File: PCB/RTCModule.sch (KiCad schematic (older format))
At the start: 0 parts

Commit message: Updated the schematic for the RTC and controller
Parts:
- added Q? (x7): IRLML2502, Micro3, symbol IRLML2502
- added Q?: NOPOP, Micro3, symbol IRLML2502
- added R? (x7): 10K, symbol R
- added R? (x2): 1K5, symbol R
- added R? (x5): 4K7, symbol R
- added R? (x2): NOPOP, symbol R
- added U?: RTC-DCF77, symbol RTC-DCF77
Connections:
- new net: Q?.3 (D), R?.2
- new net ALARM_INT: Q?.2 (S), Q?.3 (D), R?.2, R?.2, U?.10 (MOSI)
- new net DCF_RCPT: Q?.2 (S), Q?.3 (D), R?.2, R?.2, U?.8 (~SS)
- new net GND: U?.12 (GND), U?.6 (GND)
- new net MISO: Q?.2 (S), Q?.3 (D), R?.2, R?.2, U?.5 (Tx)
- new net MOSI: Q?.2 (S), Q?.3 (D), R?.2, R?.2, U?.4 (Rx)
- new net Periodic_INT: Q?.2 (S), Q?.3 (D), R?.2, R?.2
- new net Rx: Q?.2 (S), R?.2, U?.9 (SCK)
- new net SCK: Q?.2 (S), Q?.3 (D), R?.2, R?.2, U?.3 (SCL)
- new net Vbb: Q?.1 (G), Q?.1 (G), Q?.1 (G), Q?.1 (G), Q?.1 (G), Q?.1 (G), Q?.1 (G), Q?.1 (G), R?.1, R?.1, R?.1, R?.1, R?.1, R?.1, R?.1, R?.1, U?.1 (+Vb), U?.7 (+Vb)
- new net Vcc: R?.1, R?.1, R?.1, R?.1, R?.1, R?.1, R?.1, R?.1
- new net ~SS: Q?.2 (S), Q?.3 (D), R?.2, R?.2, U?.2 (SDA)
- no-connect marks 0 -> 1
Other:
- note added: "The RTC-DCF77 is a pre-fabricated module \nthat has two 6 contact pin headers each end. \nThis does not need any representation here \nwith respect to connectors."

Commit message: Generated the Netlist and started associating footprints
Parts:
- Q401, Q402, Q403, Q404, Q405, Q406, Q407, Q408: renamed from Q?; footprint Micro3 -> tfac-footprints:Micro3
- R401, R402, R403, R404, R405, R406, R407, R408, R409, R410, R411, R412, R413, R414, R415, R416: renamed from R?; footprint (none) -> Resistors_SMD:R_0805_HandSoldering
- U401: renamed from U?; footprint (none) -> tfac-footprints:RTC-DCF
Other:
- note added: "The RTC-DCF77 is a pre-fabricated module \nthat has two 6 contact pin headers each end. \nThis does not need any representation here \nwith respect to connectors.\n\nThis will be modelled in the foot print as two 6-pole \nthrough hole connectors\n"
- note removed: "The RTC-DCF77 is a pre-fabricated module \nthat has two 6 contact pin headers each end. \nThis does not need any representation here \nwith respect to connectors."

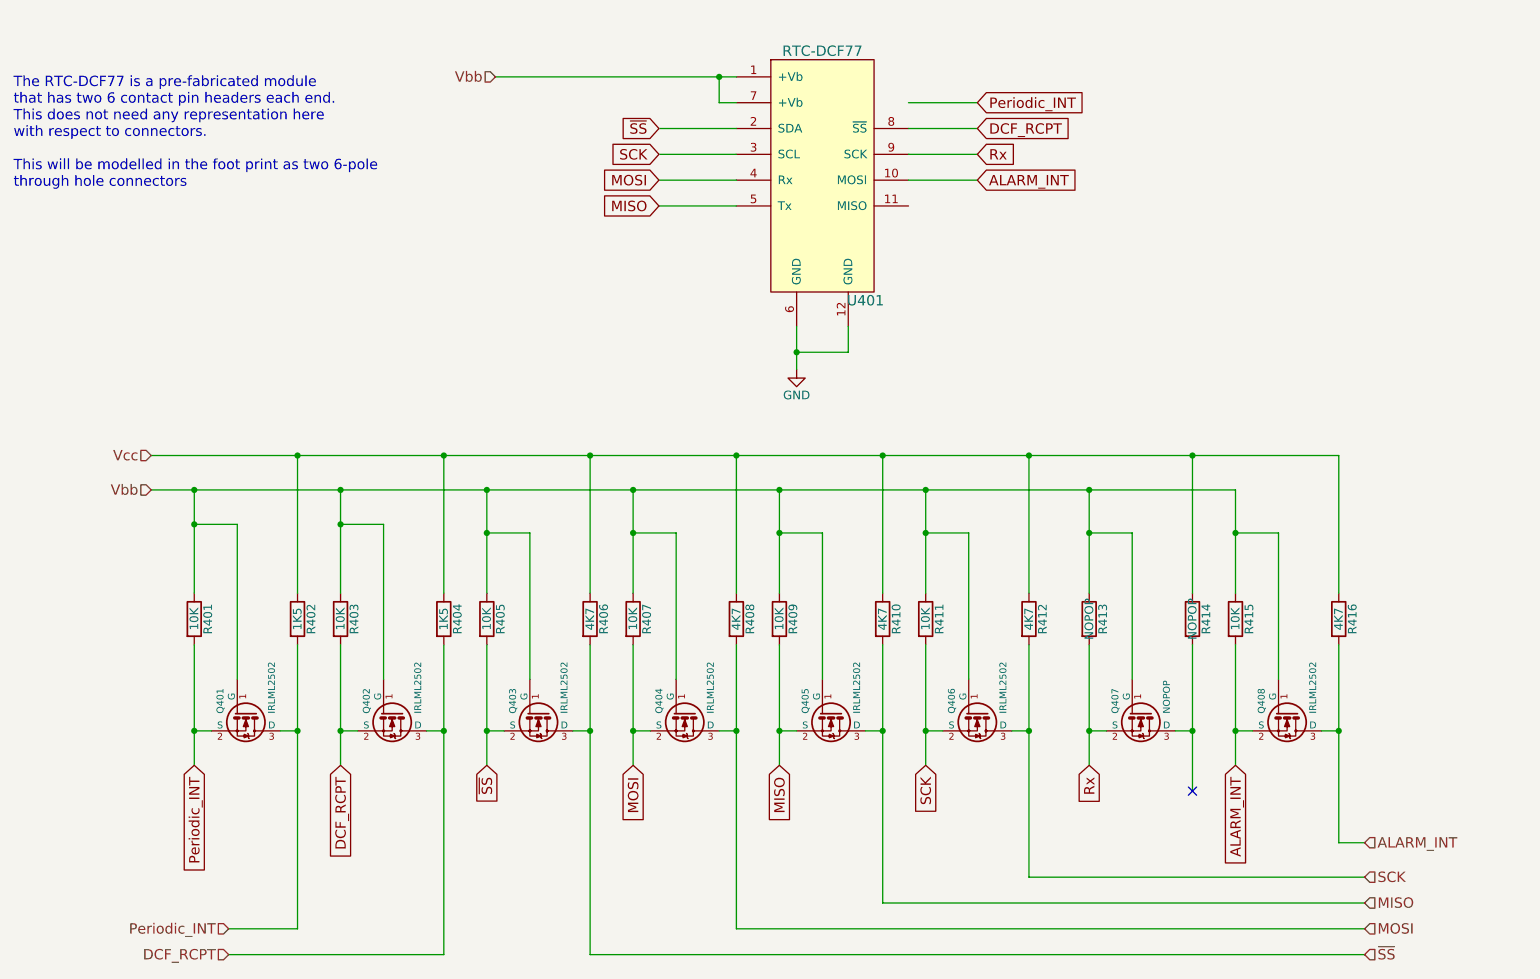
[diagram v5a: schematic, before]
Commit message: Added the switch footprints and started the layout
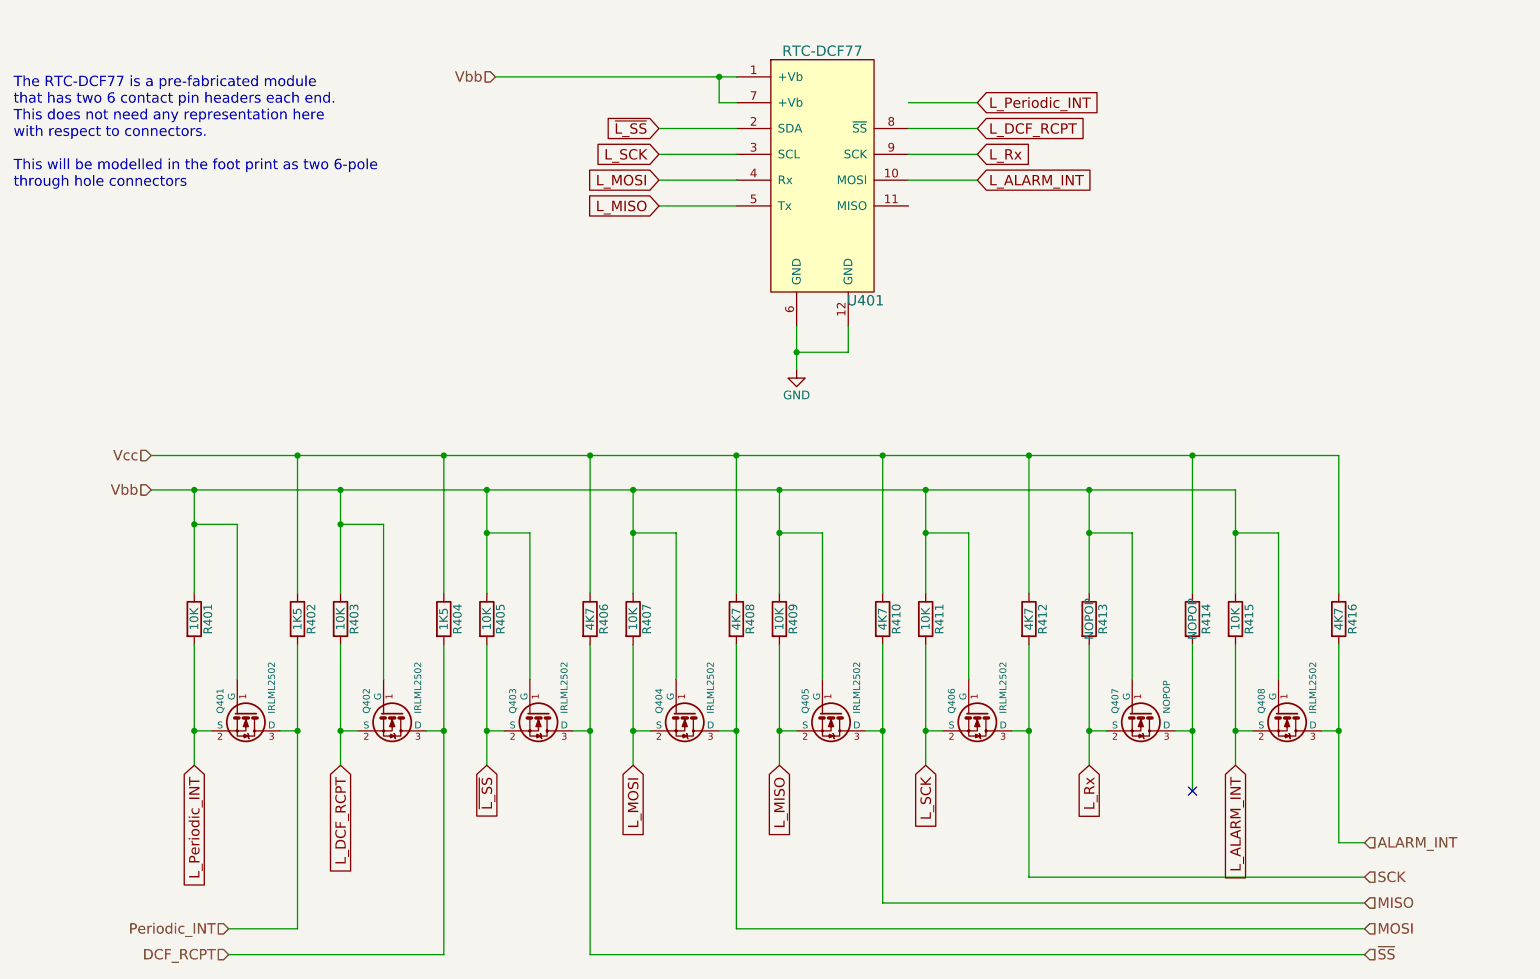
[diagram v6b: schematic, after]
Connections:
- net ALARM_INT: no longer Q408.2 (S), R415.2, U401.10 (MOSI)
- net DCF_RCPT: no longer Q402.2 (S), R403.2, U401.8 (~SS)
- net MISO: no longer Q405.2 (S), R409.2, U401.5 (Tx)
- net MOSI: no longer Q404.2 (S), R407.2, U401.4 (Rx)
- net Periodic_INT: no longer Q401.2 (S), R401.2
- net SCK: no longer Q406.2 (S), R411.2, U401.3 (SCL)
- net ~SS: no longer Q403.2 (S), R405.2, U401.2 (SDA)
- net Rx renamed L_Rx
- new net L_ALARM_INT: Q408.2 (S), R415.2, U401.10 (MOSI)
- new net L_DCF_RCPT: Q402.2 (S), R403.2, U401.8 (~SS)
- new net L_MISO: Q405.2 (S), R409.2, U401.5 (Tx)
- new net L_MOSI: Q404.2 (S), R407.2, U401.4 (Rx)
- new net L_Periodic_INT: Q401.2 (S), R401.2
- new net L_SCK: Q406.2 (S), R411.2, U401.3 (SCL)
- new net ~L_SS: Q403.2 (S), R405.2, U401.2 (SDA)
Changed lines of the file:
@@
 Vbb
 Text GLabel 2300 4950 3    60   Input ~ 0
-Periodic_INT
+L_Periodic_INT
 Text GLabel 3150 4950 3    60   Input ~ 0
-DCF_RCPT
+L_DCF_RCPT
 $Comp
 L R R405
@@
 Connection ~ 8950 4750
 Text GLabel 4000 4950 3    60   Input ~ 0
-~SS
+~L_SS
 Text GLabel 4850 4950 3    60   Input ~ 0
-MOSI
+L_MOSI
 Text GLabel 5700 4950 3    60   Input ~ 0
-MISO
+L_MISO
 Text GLabel 6550 4950 3    60   Input ~ 0
-SCK
+L_SCK
 Text GLabel 7500 4950 3    60   Input ~ 0
-Rx
+L_Rx
 Text GLabel 8350 4950 3    60   Input ~ 0
-ALARM_INT
+L_ALARM_INT
 Text GLabel 5000 1700 0    60   Input ~ 0
-MISO
+L_MISO
 Text GLabel 5000 1550 0    60   Input ~ 0
-MOSI
+L_MOSI
 Text GLabel 5000 1400 0    60   Input ~ 0
-SCK
+L_SCK
 Text GLabel 5000 1250 0    60   Input ~ 0
-~SS
+~L_SS
 Text Notes 1250 1600 0    60   ~ 0
 The RTC-DCF77 is a pre-fabricated module \nthat has two 6 contact pin headers each end. \nThis does not need any representation here \nwith respect to connectors.\n\nThis will be modelled in the foot print as two 6-pole \nthrough hole connectors\n
@@
 	6300 5750 9100 5750
 Text GLabel 6850 1100 2    60   Input ~ 0
-Periodic_INT
+L_Periodic_INT
 Text GLabel 6850 1250 2    60   Input ~ 0
-DCF_RCPT
+L_DCF_RCPT
 Text GLabel 6850 1550 2    60   Input ~ 0
-ALARM_INT
+L_ALARM_INT
 Wire Wire Line
 	6450 1100 6850 1100
@@
 	6450 1550 6850 1550
 Text GLabel 6850 1400 2    60   Input ~ 0
-Rx
+L_Rx
 Wire Wire Line
 	6450 1400 6850 1400

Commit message: Started the layout
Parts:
- added TP1, TP2: CONN_01X06, Pin_Headers:Pin_Header_Straight_1x06, symbol CONN_01X06
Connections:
- wire segments 87 -> 104
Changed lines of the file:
@@
 	4050 950  5450 950
 Wire Wire Line
-	5350 950  5350 1100
+	5350 600  5350 1100
 Wire Wire Line
 	5350 1100 5450 1100
@@
 	6450 1400 6850 1400
 NoConn ~ 8100 5100
+$Comp
+L CONN_01X06 TP1
+U 1 1 55D23692
+P 9400 1350
+F 0 "TP1" H 9400 1700 50  0000 C CNN
+F 1 "CONN_01X06" V 9500 1350 50  0000 C CNN
+F 2 "Pin_Headers:Pin_Header_Straight_1x06" H 9400 1350 60  0001 C CNN
+F 3 "" H 9400 1350 60  0000 C CNN
+	1    9400 1350
+	1    0    0    -1
+$EndComp
+$Comp
+L CONN_01X06 TP2
+U 1 1 55D23781
+P 9450 2450
+F 0 "TP2" H 9450 2800 50  0000 C CNN
+F 1 "CONN_01X06" V 9550 2450 50  0000 C CNN
+F 2 "Pin_Headers:Pin_Header_Straight_1x06" H 9450 2450 60  0001 C CNN
+F 3 "" H 9450 2450 60  0000 C CNN
+	1    9450 2450
+	1    0    0    -1
+$EndComp
+Text GLabel 9000 1200 0    60   Input ~ 0
+~L_SS
+Text GLabel 9000 1300 0    60   Input ~ 0
+L_SCK
+Text GLabel 9000 1400 0    60   Input ~ 0
+L_MOSI
+Text GLabel 9000 1500 0    60   Input ~ 0
+L_MISO
+$Comp
+L GND #PWR07
+U 1 1 55D23BA4
+P 8900 1700
+F 0 "#PWR07" H 8900 1450 50  0001 C CNN
+F 1 "GND" H 8900 1550 50  0000 C CNN
+F 2 "" H 8900 1700 60  0000 C CNN
+F 3 "" H 8900 1700 60  0000 C CNN
+	1    8900 1700
+	1    0    0    -1
+$EndComp
+Wire Wire Line
+	9200 1600 8900 1600
+Wire Wire Line
+	8900 1600 8900 1700
+Wire Wire Line
+	9200 1500 9000 1500
+Wire Wire Line
+	9200 1400 9000 1400
+Wire Wire Line
+	9200 1300 9000 1300
+Wire Wire Line
+	9200 1200 9000 1200
+Text GLabel 9050 2300 0    60   Input ~ 0
+L_Periodic_INT
+Text GLabel 9050 2400 0    60   Input ~ 0
+L_DCF_RCPT
+Text GLabel 9050 2500 0    60   Input ~ 0
+L_Rx
+Text GLabel 9050 2600 0    60   Input ~ 0
+L_ALARM_INT
+$Comp
+L GND #PWR08
+U 1 1 55D24A11
+P 9050 2850
+F 0 "#PWR08" H 9050 2600 50  0001 C CNN
+F 1 "GND" H 9050 2700 50  0000 C CNN
+F 2 "" H 9050 2850 60  0000 C CNN
+F 3 "" H 9050 2850 60  0000 C CNN
+	1    9050 2850
+	1    0    0    -1
+$EndComp
+Wire Wire Line
+	9250 2700 9050 2700
+Wire Wire Line
+	9050 2700 9050 2850
+Wire Wire Line
+	9250 2600 9050 2600
+Wire Wire Line
+	9250 2500 9050 2500
+Wire Wire Line
+	9250 2400 9050 2400
+Wire Wire Line
+	9250 2300 9050 2300
+Wire Wire Line
+	9200 600  9200 1100
+Wire Wire Line
+	9750 600  9750 1950
+Wire Wire Line
+	9750 1950 9250 1950
+Wire Wire Line
+	9250 1950 9250 2200
+Connection ~ 9200 600
+Wire Wire Line
+	5350 600  9750 600
 $EndSCHEMATC
